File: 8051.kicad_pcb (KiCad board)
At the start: 2 copper layers, 99.1 x 49.9 mm, 15 parts, among them J1 Conn_01x39, J2 S1 S2, J3 PORT1, U1 DS80C320, U2 74LS08, U3 74LS04, U4 74LS373, Y1 Crystal

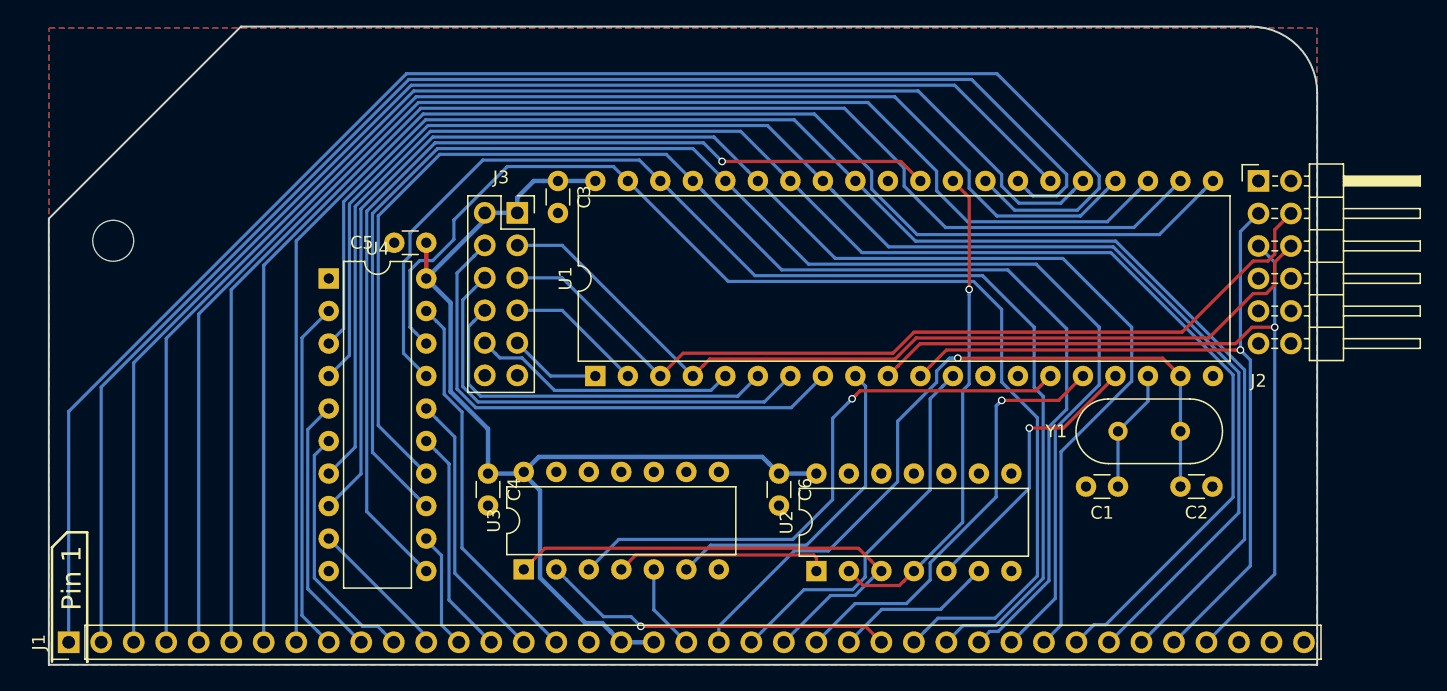
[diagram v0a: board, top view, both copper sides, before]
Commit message: Upgrade Kicad projects to v6
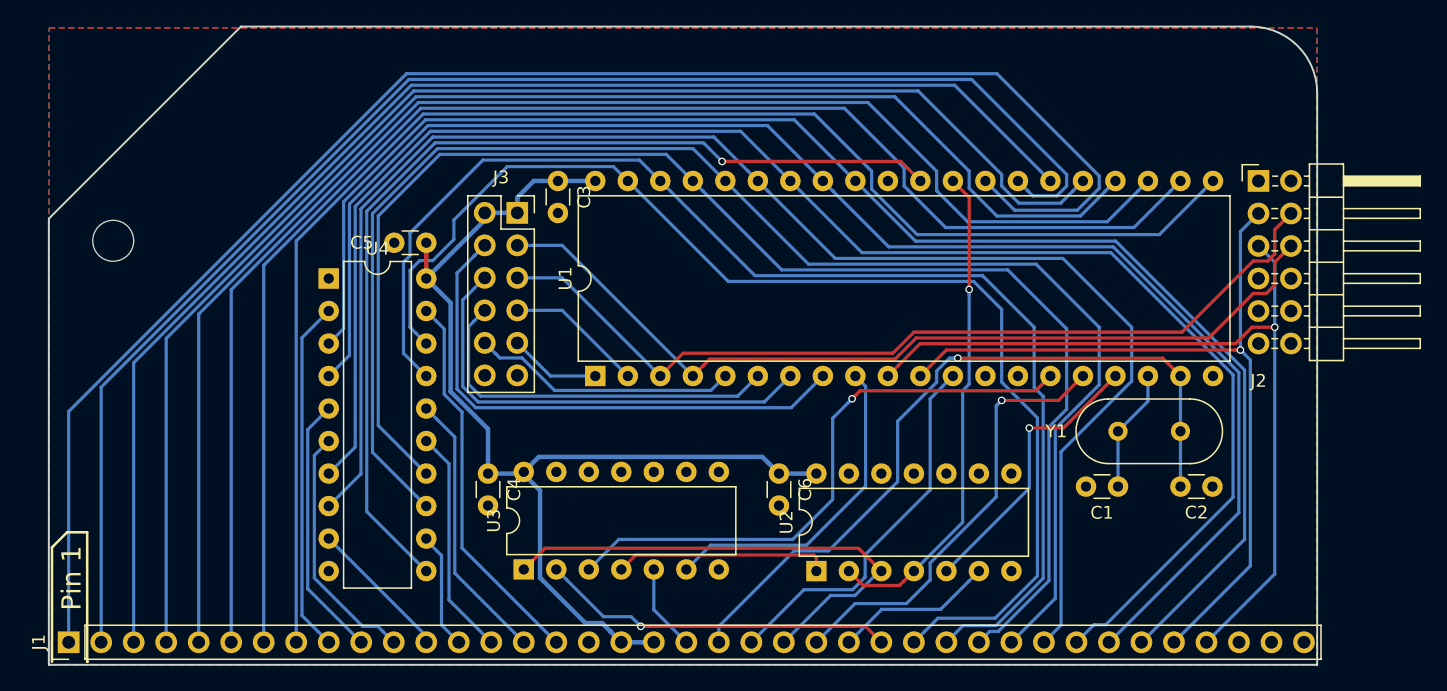
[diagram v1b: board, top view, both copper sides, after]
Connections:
- net /~INT renamed /~{INT}
- net /~IORQ renamed /~{IORQ}
- net /~MREQ renamed /~{MREQ}
- net /~RD renamed /~{RD}
- net /~RST renamed /~{RST}
- net /~WR renamed /~{WR}
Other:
- net class Default removed
- net class Power removed
